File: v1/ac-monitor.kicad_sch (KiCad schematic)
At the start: 3 parts, among them U6 MID400

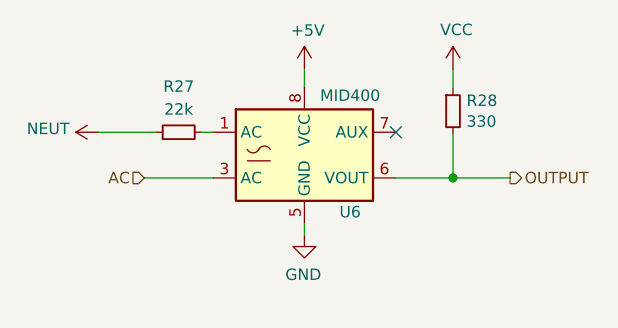
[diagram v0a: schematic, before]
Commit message: add vaux cap to mid400
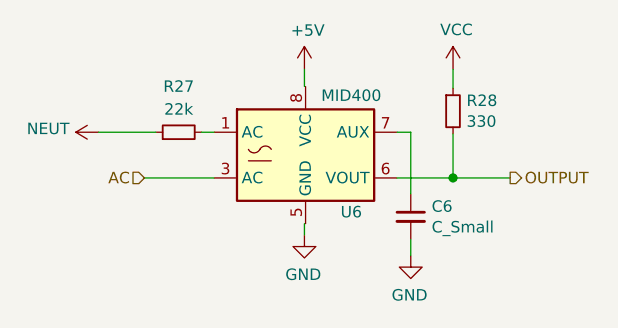
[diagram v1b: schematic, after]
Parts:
- added C6: C_Small, Capacitor_SMD:C_0603_1608Metric_Pad1.05x0.95mm_HandSolder, symbol Device:C_Small
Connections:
- net +5V: no longer U6.8 (VCC)
- net GND: now also C6.2; no longer U6.5 (GND)
- net at U6.7 (AUX): now also C6.1
- no-connect marks 1 -> 0
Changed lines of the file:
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@@
   (paper "A5")
   (junction (at 120.015 71.12) (diameter 1.016) (color 0 0 0 0))
-  (no_connect (at 113.665 66.04))
   (wire (pts (xy 80.645 66.04) (xy 86.995 66.04))
     (stroke (width 0) (type solid) (color 0 0 0 0))
   )
-  (wire (pts (xy 85.725 71.12) (xy 93.345 71.12))
+  (wire (pts (xy 85.725 71.12) (xy 93.472 71.12))
     (stroke (width 0) (type solid) (color 0 0 0 0))
   )
-  (wire (pts (xy 92.075 66.04) (xy 93.345 66.04))
+  (wire (pts (xy 92.075 66.04) (xy 93.472 66.04))
     (stroke (width 0) (type solid) (color 0 0 0 0))
   )
@@
     (stroke (width 0) (type solid) (color 0 0 0 0))
   )
-  (wire (pts (xy 113.665 71.12) (xy 120.015 71.12))
+  (wire (pts (xy 113.792 66.04) (xy 115.316 66.04))
+    (stroke (width 0) (type solid) (color 0 0 0 0))
+  )
+  (wire (pts (xy 113.792 71.12) (xy 120.015 71.12))
+    (stroke (width 0) (type solid) (color 0 0 0 0))
+  )
+  (wire (pts (xy 115.316 66.04) (xy 115.316 72.898))
+    (stroke (width 0) (type solid) (color 0 0 0 0))
+  )
+  (wire (pts (xy 115.316 77.978) (xy 115.316 79.756))
     (stroke (width 0) (type solid) (color 0 0 0 0))
   )
@@
   (symbol (lib_id "power:NEUT") (at 80.645 66.04 90)
     (in_bom yes) (on_board yes)
-    (property "Reference" "#PWR041" (id 0) (at 84.455 66.04 0)
+    (property "Reference" "#PWR037" (id 0) (at 84.455 66.04 0)
       (effects (font (size 1.27 1.27)) hide)
     )
@@
   (symbol (lib_id "power:+5V") (at 103.505 59.055 0)
     (in_bom yes) (on_board yes)
-    (property "Reference" "#PWR042" (id 0) (at 103.505 62.865 0)
+    (property "Reference" "#PWR038" (id 0) (at 103.505 62.865 0)
       (effects (font (size 1.27 1.27)) hide)
     )
@@
   (symbol (lib_id "power:VCC") (at 120.015 59.055 0)
     (in_bom yes) (on_board yes)
-    (property "Reference" "#PWR044" (id 0) (at 120.015 62.865 0)
+    (property "Reference" "#PWR040" (id 0) (at 120.015 62.865 0)
       (effects (font (size 1.27 1.27)) hide)
     )
@@
   (symbol (lib_id "power:GND") (at 103.505 77.47 0) (mirror y)
     (in_bom yes) (on_board yes)
-    (property "Reference" "#PWR043" (id 0) (at 103.505 83.82 0)
+    (property "Reference" "#PWR039" (id 0) (at 103.505 83.82 0)
       (effects (font (size 1.27 1.27)) hide)
     )
@@
     )
     (property "Datasheet" "" (id 3) (at 103.505 77.47 0)
+      (effects (font (size 1.27 1.27)) hide)
+    )
+  )
+  (symbol (lib_id "power:GND") (at 115.316 79.756 0) (mirror y)
+    (in_bom yes) (on_board yes)
+    (property "Reference" "#PWR0103" (id 0) (at 115.316 86.106 0)
+      (effects (font (size 1.27 1.27)) hide)
+    )
+    (property "Value" "GND" (id 1) (at 115.189 84.1502 0))
+    (property "Footprint" "" (id 2) (at 115.316 79.756 0)
+      (effects (font (size 1.27 1.27)) hide)
+    )
+    (property "Datasheet" "" (id 3) (at 115.316 79.756 0)
       (effects (font (size 1.27 1.27)) hide)
     )
@@
     )
   )
-  (symbol (lib_id "Isolator:MID400") (at 103.505 68.58 0)
+  (symbol (lib_id "Device:C_Small") (at 115.316 75.438 0)
     (in_bom yes) (on_board yes)
-    (property "Reference" "U6" (id 0) (at 108.585 74.9108 0))
-    (property "Value" "MID400" (id 1) (at 108.585 61.9695 0))
-    (property "Footprint" "Package_DIP:DIP-8_W7.62mm" (id 2) (at 103.505 68.58 0)
+    (property "Reference" "C6" (id 0) (at 117.6402 74.2886 0)
+      (effects (font (size 1.27 1.27)) (justify left))
+    )
+    (property "Value" "C_Small" (id 1) (at 117.6402 76.5873 0)
+      (effects (font (size 1.27 1.27)) (justify left))
+    )
+    (property "Footprint" "Capacitor_SMD:C_0603_1608Metric_Pad1.05x0.95mm_HandSolder" (id 2) (at 115.316 75.438 0)
       (effects (font (size 1.27 1.27)) hide)
     )
-    (property "Datasheet" "https://www.onsemi.com/pub/Collateral/MID400-D.pdf" (id 3) (at 103.505 68.58 0)
+    (property "Datasheet" "~" (id 3) (at 115.316 75.438 0)
       (effects (font (size 1.27 1.27)) hide)
     )
+  )
+  (symbol (lib_id "Isolator:MID400") (at 103.632 68.58 0)
+    (in_bom yes) (on_board yes)
+    (property "Reference" "U6" (id 0) (at 108.712 74.9108 0))
+    (property "Value" "MID400" (id 1) (at 108.712 61.9695 0))
+    (property "Footprint" "Package_DIP:DIP-8_W7.62mm" (id 2) (at 103.632 68.58 0)
+      (effects (font (size 1.27 1.27)) hide)
+    )
+    (property "Datasheet" "https://www.onsemi.com/pub/Collateral/MID400-D.pdf" (id 3) (at 103.632 68.58 0)
+      (effects (font (size 1.27 1.27)) hide)
+    )

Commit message: cleanups
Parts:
- C6: value C_Small -> DNP
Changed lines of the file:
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@@
       (effects (font (size 1.27 1.27)) (justify left))
     )
-    (property "Value" "C_Small" (id 1) (at 117.6402 76.5873 0)
+    (property "Value" "DNP" (id 1) (at 117.6528 76.581 0)
       (effects (font (size 1.27 1.27)) (justify left))
     )

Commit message: cosmetics
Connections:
- net +5V: now also U6.8 (VCC)
- net GND: now also U6.5 (GND)

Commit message: final touches for v1
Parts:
- renumbered C6 to C7, R27 to R29, R28 to R30, U6 to U7
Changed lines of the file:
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@@
   (symbol (lib_id "power:NEUT") (at 80.645 66.294 90)
     (in_bom yes) (on_board yes)
-    (property "Reference" "#PWR037" (id 0) (at 84.455 66.294 0)
+    (property "Reference" "#PWR041" (id 0) (at 84.455 66.294 0)
       (effects (font (size 1.27 1.27)) hide)
     )
@@
   (symbol (lib_id "power:+5V") (at 103.632 59.309 0)
     (in_bom yes) (on_board yes)
-    (property "Reference" "#PWR038" (id 0) (at 103.632 63.119 0)
+    (property "Reference" "#PWR042" (id 0) (at 103.632 63.119 0)
       (effects (font (size 1.27 1.27)) hide)
     )
@@
   (symbol (lib_id "power:VCC") (at 120.015 59.309 0)
     (in_bom yes) (on_board yes)
-    (property "Reference" "#PWR040" (id 0) (at 120.015 63.119 0)
+    (property "Reference" "#PWR044" (id 0) (at 120.015 63.119 0)
       (effects (font (size 1.27 1.27)) hide)
     )
@@
   (symbol (lib_id "power:GND") (at 103.632 77.724 0) (mirror y)
     (in_bom yes) (on_board yes)
-    (property "Reference" "#PWR039" (id 0) (at 103.632 84.074 0)
+    (property "Reference" "#PWR043" (id 0) (at 103.632 84.074 0)
       (effects (font (size 1.27 1.27)) hide)
     )
@@
   (symbol (lib_id "power:GND") (at 115.316 80.01 0) (mirror y)
     (in_bom yes) (on_board yes)
-    (property "Reference" "#PWR0103" (id 0) (at 115.316 86.36 0)
+    (property "Reference" "#PWR0104" (id 0) (at 115.316 86.36 0)
       (effects (font (size 1.27 1.27)) hide)
     )
@@
   (symbol (lib_id "Device:R_Small") (at 89.535 66.294 90)
     (in_bom yes) (on_board yes)
-    (property "Reference" "R27" (id 0) (at 89.535 61.214 90))
+    (property "Reference" "R29" (id 0) (at 89.535 61.214 90))
     (property "Value" "22k" (id 1) (at 89.535 63.754 90))
     (property "Footprint" "Resistor_SMD:R_0603_1608Metric_Pad1.05x0.95mm_HandSolder" (id 2) (at 89.535 66.294 0)
@@
   (symbol (lib_id "Device:R_Small") (at 120.015 63.9572 0)
     (in_bom yes) (on_board yes)
-    (property "Reference" "R28" (id 0) (at 121.5136 62.7888 0)
+    (property "Reference" "R30" (id 0) (at 121.5136 62.7888 0)
       (effects (font (size 1.27 1.27)) (justify left))
     )
@@
   (symbol (lib_id "Device:C_Small") (at 115.316 75.692 0)
     (in_bom yes) (on_board yes)
-    (property "Reference" "C6" (id 0) (at 117.6402 74.5426 0)
+    (property "Reference" "C7" (id 0) (at 117.6402 74.5426 0)
       (effects (font (size 1.27 1.27)) (justify left))
     )
@@
   (symbol (lib_id "Isolator:MID400") (at 103.632 68.834 0)
     (in_bom yes) (on_board yes)
-    (property "Reference" "U6" (id 0) (at 108.712 75.1648 0))
+    (property "Reference" "U7" (id 0) (at 108.712 75.1648 0))
     (property "Value" "MID400" (id 1) (at 108.712 62.2235 0))
     (property "Footprint" "Package_DIP:DIP-8_W7.62mm" (id 2) (at 103.632 68.834 0)
